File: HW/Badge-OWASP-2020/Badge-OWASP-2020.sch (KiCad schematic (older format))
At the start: 28 parts, among them J1 Shitty Add-Ons, J2 Battery, J3 I2C, J4 USB_B, Q1 MMBT3904, Q2 DMG3415U-7, Q3 MMBT3904, SW1 RST, SW2 BOOT, U1 ESP32-WROOM-32, U2 CH340C, U3 AP111733

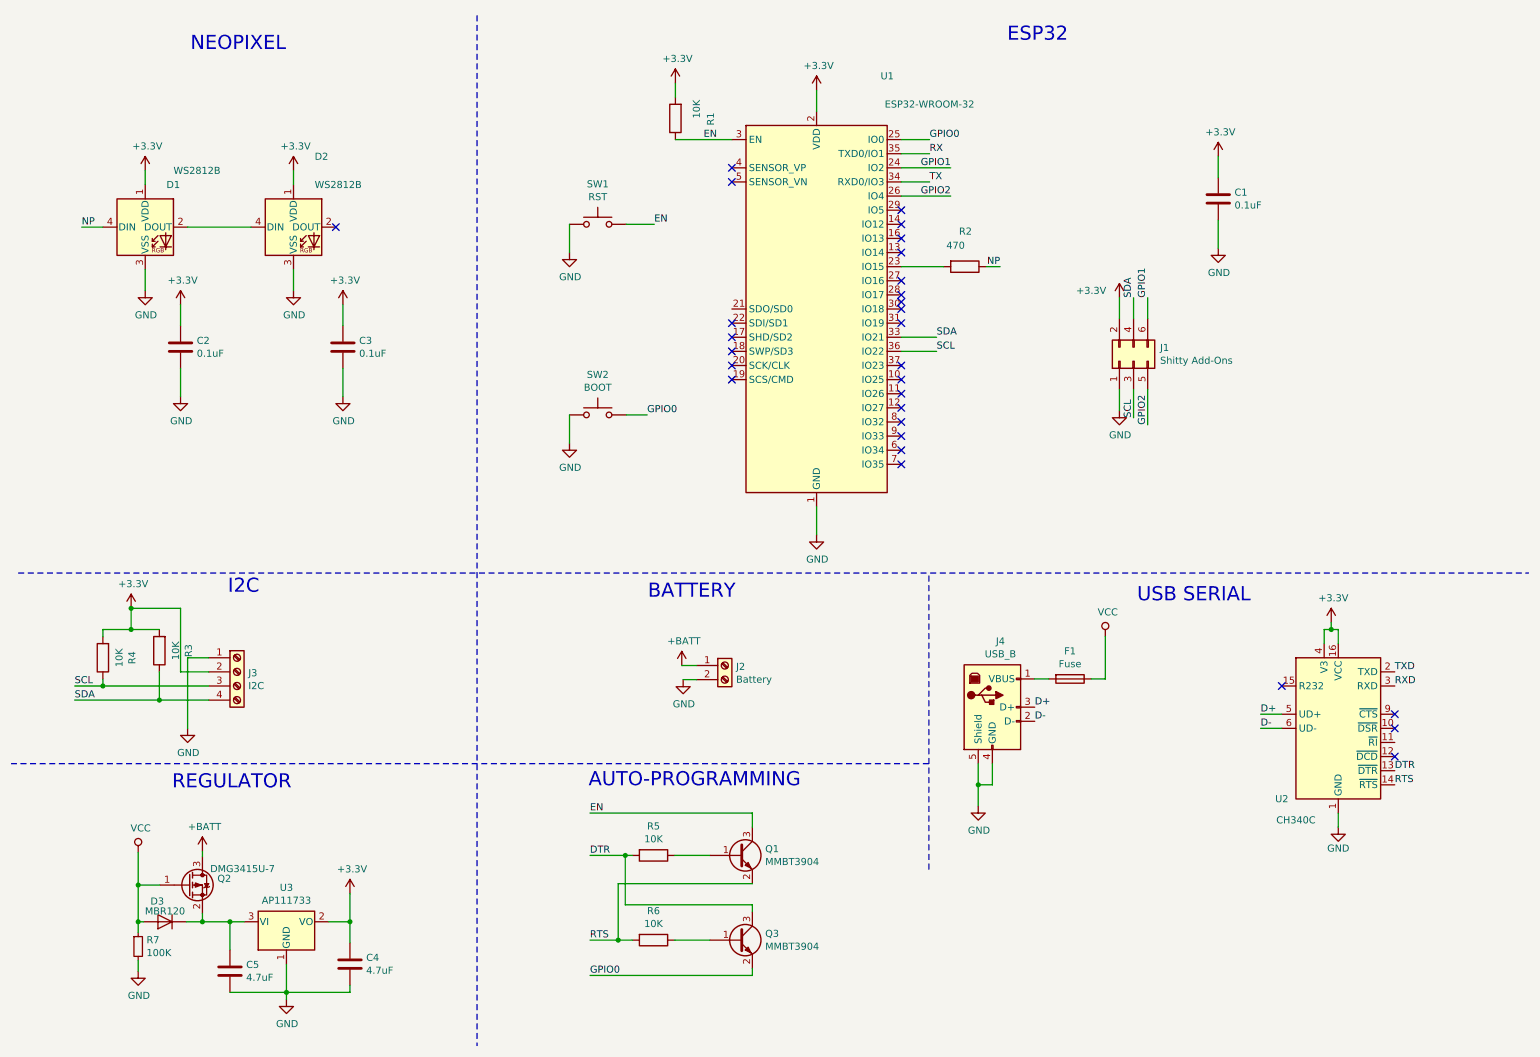
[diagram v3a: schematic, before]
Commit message: fix GPIO1 for shitty adons with neopixel
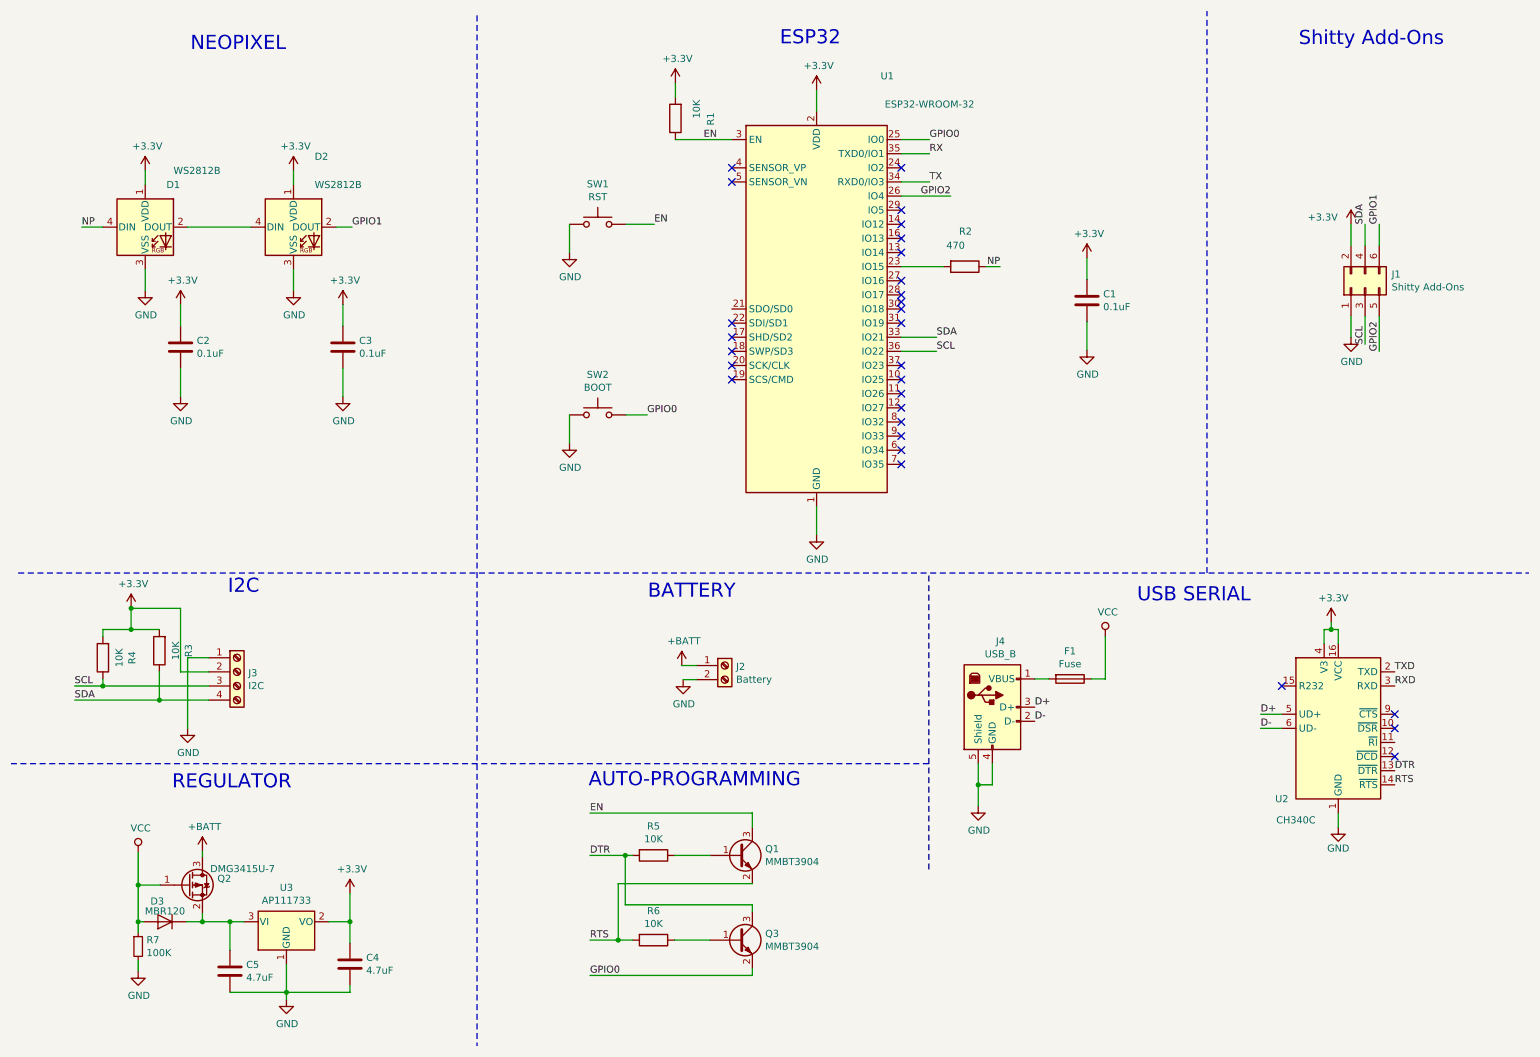
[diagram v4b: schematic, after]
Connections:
- net GPIO1: now also D2.2 (DOUT); no longer U1.24 (IO2)
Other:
- note added: "Shitty Add-Ons"
- moved on the sheet: C1, J1
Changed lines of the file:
@@
 Wire Wire Line
 	1100 2000 950  2000
-NoConn ~ 2750 2000
 Wire Notes Line
 	500  4450 11200 4450
@@
 L Device:C C1
 U 1 1 5DFBF1D5
-P 9000 1800
-F 0 "C1" H 9115 1846 50  0000 L CNN
-F 1 "0.1uF" H 9115 1755 50  0000 L CNN
-F 2 "Capacitor_SMD:C_0805_2012Metric_Pad1.15x1.40mm_HandSolder" H 9038 1650 50  0001 C CNN
-F 3 "~" H 9000 1800 50  0001 C CNN
-	1    9000 1800
+P 8070 2520
+F 0 "C1" H 8185 2566 50  0000 L CNN
+F 1 "0.1uF" H 8185 2475 50  0000 L CNN
+F 2 "Capacitor_SMD:C_0805_2012Metric_Pad1.15x1.40mm_HandSolder" H 8108 2370 50  0001 C CNN
+F 3 "~" H 8070 2520 50  0001 C CNN
+	1    8070 2520
 	1    0    0    -1
 $EndComp
@@
 L power:GND #PWR06
 U 1 1 5DFBF1E1
-P 9000 2150
-F 0 "#PWR06" H 9000 1900 50  0001 C CNN
-F 1 "GND" H 9005 1977 50  0000 C CNN
-F 2 "" H 9000 2150 50  0001 C CNN
-F 3 "" H 9000 2150 50  0001 C CNN
-	1    9000 2150
-	1    0    0    -1
-$EndComp
-Wire Wire Line
-	9000 1950 9000 2150
-Wire Wire Line
-	9000 1650 9000 1500
+P 8070 2870
+F 0 "#PWR06" H 8070 2620 50  0001 C CNN
+F 1 "GND" H 8075 2697 50  0000 C CNN
+F 2 "" H 8070 2870 50  0001 C CNN
+F 3 "" H 8070 2870 50  0001 C CNN
+	1    8070 2870
+	1    0    0    -1
+$EndComp
+Wire Wire Line
+	8070 2670 8070 2870
+Wire Wire Line
+	8070 2370 8070 2220
 $Comp
 L power:+3.3V #PWR02
@@
 Wire Wire Line
 	7055 2280 6755 2280
-Wire Wire Line
-	6755 1580 7105 1580
-Text Label 7105 1580 2    50   ~ 0
-GPIO1
 Text Label 7105 1780 2    50   ~ 0
 GPIO2
@@
 NoConn ~ 5555 2680
 Wire Wire Line
-	8500 2650 8500 2500
-Wire Wire Line
-	8500 3150 8500 3400
-Text Label 8500 3400 1    50   ~ 0
+	10140 2130 10140 1980
+Wire Wire Line
+	10140 2630 10140 2880
+Text Label 10140 2880 1    50   ~ 0
 GPIO2
-Text Label 8500 2500 1    50   ~ 0
+Text Label 10140 1980 1    50   ~ 0
 GPIO1
 Wire Wire Line
-	8400 3150 8400 3350
-Wire Wire Line
-	8400 2500 8400 2650
-Text Label 8400 3350 1    50   ~ 0
+	10040 2630 10040 2830
+Wire Wire Line
+	10040 1980 10040 2130
+Text Label 10040 2830 1    50   ~ 0
 SCL
-Text Label 8400 2500 1    50   ~ 0
+Text Label 10040 1980 1    50   ~ 0
 SDA
 Wire Wire Line
-	8300 3300 8300 3150
-Wire Wire Line
-	8300 2500 8300 2650
+	9940 2780 9940 2630
+Wire Wire Line
+	9940 1980 9940 2130
 $Comp
 L power:GND #PWR015
 U 1 1 5DFE9B12
-P 8300 3300
-F 0 "#PWR015" H 8300 3050 50  0001 C CNN
-F 1 "GND" H 8305 3127 50  0000 C CNN
-F 2 "" H 8300 3300 50  0001 C CNN
-F 3 "" H 8300 3300 50  0001 C CNN
-	1    8300 3300
+P 9940 2780
+F 0 "#PWR015" H 9940 2530 50  0001 C CNN
+F 1 "GND" H 9945 2607 50  0000 C CNN
+F 2 "" H 9940 2780 50  0001 C CNN
+F 3 "" H 9940 2780 50  0001 C CNN
+	1    9940 2780
 	1    0    0    -1
 $EndComp
@@
 L Connector_Generic:Conn_02x03_Odd_Even J1
 U 1 1 5DFE251B
-P 8400 2950
-F 0 "J1" V 8496 2762 50  0000 R CNN
-F 1 "Shitty Add-Ons" V 8405 2762 50  0000 R CNN
-F 2 "Connector_PinHeader_2.54mm:PinHeader_2x03_P2.54mm_Vertical" H 8400 2950 50  0001 C CNN
-F 3 "~" H 8400 2950 50  0001 C CNN
-	1    8400 2950
+P 10040 2430
+F 0 "J1" V 10136 2242 50  0000 R CNN
+F 1 "Shitty Add-Ons" V 10045 2242 50  0000 R CNN
+F 2 "Connector_PinHeader_2.54mm:PinHeader_2x03_P2.54mm_Vertical" H 10040 2430 50  0001 C CNN
+F 3 "~" H 10040 2430 50  0001 C CNN
+	1    10040 2430
 	0    -1   -1   0
 $EndComp
@@
 L power:+3.3V #PWR010
 U 1 1 5DFBF1DB
-P 8300 2500
-F 0 "#PWR010" H 8300 2350 50  0001 C CNN
-F 1 "+3.3V" H 8100 2550 50  0000 C CNN
-F 2 "" H 8300 2500 50  0001 C CNN
-F 3 "" H 8300 2500 50  0001 C CNN
-	1    8300 2500
+P 9940 1980
+F 0 "#PWR010" H 9940 1830 50  0001 C CNN
+F 1 "+3.3V" H 9740 2030 50  0000 C CNN
+F 2 "" H 9940 1980 50  0001 C CNN
+F 3 "" H 9940 1980 50  0001 C CNN
+	1    9940 1980
 	1    0    0    -1
 $EndComp
@@
 L power:+3.3V #PWR03
 U 1 1 5E03555F
-P 9000 1500
-F 0 "#PWR03" H 9000 1350 50  0001 C CNN
-F 1 "+3.3V" H 9015 1673 50  0000 C CNN
-F 2 "" H 9000 1500 50  0001 C CNN
-F 3 "" H 9000 1500 50  0001 C CNN
-	1    9000 1500
+P 8070 2220
+F 0 "#PWR03" H 8070 2070 50  0001 C CNN
+F 1 "+3.3V" H 8085 2393 50  0000 C CNN
+F 2 "" H 8070 2220 50  0001 C CNN
+F 3 "" H 8070 2220 50  0001 C CNN
+	1    8070 2220
 	1    0    0    -1
 $EndComp
@@
 Text Notes 1720 760  0    100  ~ 0
 NEOPIXEL
-Text Notes 7505 695  0    100  ~ 0
+Text Notes 5895 720  0    100  ~ 0
 ESP32
 Text Notes 1590 5990 0    100  ~ 0
@@
 	1    0    0    -1
 $EndComp
+Wire Notes Line
+	8920 4450 8920 470
+Text Notes 9570 725  0    100  ~ 0
+Shitty Add-Ons
+Wire Wire Line
+	2750 2000 2865 2000
+Text Label 2865 2000 0    50   ~ 0
+GPIO1
+NoConn ~ 6755 1580
 $EndSCHEMATC

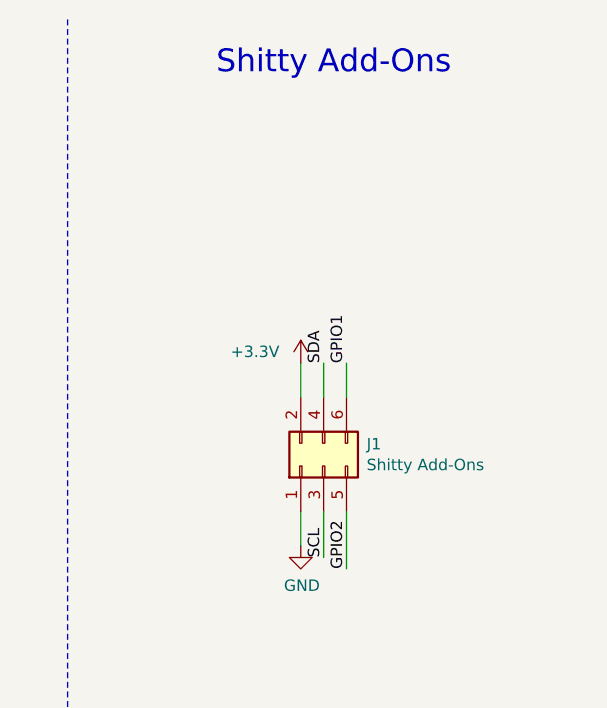
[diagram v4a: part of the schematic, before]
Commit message: correct pinout sao1.69bis
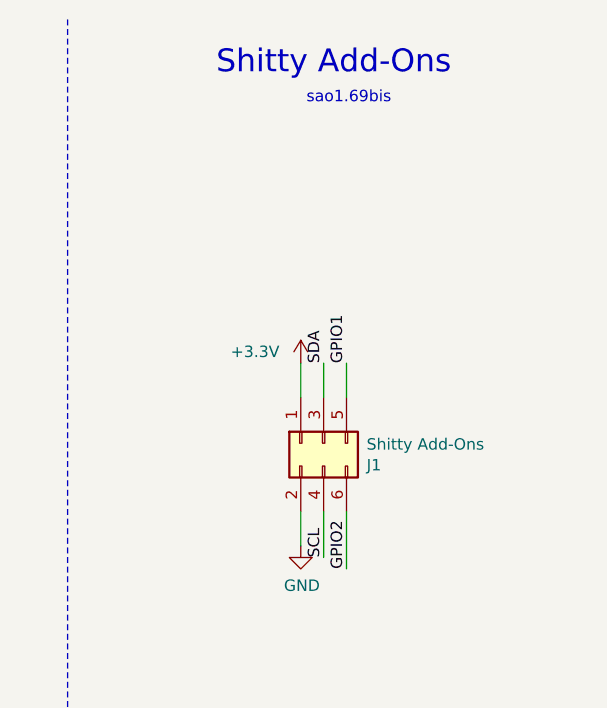
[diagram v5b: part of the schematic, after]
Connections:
- net +3V3: now also J1.1 (Pin_1); no longer J1.2 (Pin_2)
- net GND: now also J1.2 (Pin_2); no longer J1.1 (Pin_1)
- net GPIO1: now also J1.5 (Pin_5); no longer J1.6 (Pin_6)
- net GPIO2: now also J1.6 (Pin_6); no longer J1.5 (Pin_5)
- net SCL: now also J1.4 (Pin_4); no longer J1.3 (Pin_3)
- net SDA: now also J1.3 (Pin_3); no longer J1.4 (Pin_4)
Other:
- note added: "sao1.69bis"
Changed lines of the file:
@@
 Wire Wire Line
 	10140 2130 10140 1980
-Wire Wire Line
-	10140 2630 10140 2880
 Text Label 10140 2880 1    50   ~ 0
 GPIO2
 Text Label 10140 1980 1    50   ~ 0
 GPIO1
-Wire Wire Line
-	10040 2630 10040 2830
 Wire Wire Line
 	10040 1980 10040 2130
@@
 Text Label 10040 1980 1    50   ~ 0
 SDA
-Wire Wire Line
-	9940 2780 9940 2630
 Wire Wire Line
 	9940 1980 9940 2130
@@
 	1    9940 2780
 	1    0    0    -1
-$EndComp
-$Comp
-L Connector_Generic:Conn_02x03_Odd_Even J1
-U 1 1 5DFE251B
-P 10040 2430
-F 0 "J1" V 10136 2242 50  0000 R CNN
-F 1 "Shitty Add-Ons" V 10045 2242 50  0000 R CNN
-F 2 "Connector_PinHeader_2.54mm:PinHeader_2x03_P2.54mm_Vertical" H 10040 2430 50  0001 C CNN
-F 3 "~" H 10040 2430 50  0001 C CNN
-	1    10040 2430
-	0    -1   -1   0
 $EndComp
 $Comp
@@
 GPIO1
 NoConn ~ 6755 1580
+$Comp
+L Connector_Generic:Conn_02x03_Odd_Even J1
+U 1 1 5DFE251B
+P 10040 2330
+F 0 "J1" V 10136 2142 50  0000 R CNN
+F 1 "Shitty Add-Ons" V 10045 2142 50  0000 R CNN
+F 2 "Connector_PinHeader_2.54mm:PinHeader_2x03_P2.54mm_Vertical" H 10040 2330 50  0001 C CNN
+F 3 "~" H 10040 2330 50  0001 C CNN
+	1    10040 2330
+	0    -1   1    0
+$EndComp
+Wire Wire Line
+	9940 2630 9940 2780
+Wire Wire Line
+	10040 2630 10040 2830
+Wire Wire Line
+	10140 2630 10140 2880
+Text Notes 9965 850  0    50   ~ 0
+sao1.69bis
 $EndSCHEMATC
